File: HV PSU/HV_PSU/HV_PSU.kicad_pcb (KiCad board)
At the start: 2 copper layers, 200 x 80 mm, 104 parts, among them J1 Screw_Terminal_01x07, J13 MountingHole_Pad, J2 AC_HV_1, J3 AC_HV_2, J4 MountingHole_Pad, J5 AC_HV_2, Q1 2N7002, Q2 IRFS4227, Q3 IRFS4227, T1 UY12, U1 L7812, U2 TPS2814D

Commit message: backup
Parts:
- added C19: 330n, Capacitor_THT:C_Rect_L18.0mm_W9.0mm_P15.00mm_FKS3_FKP3, B.Cu at (11.5, 41.5)
- renumbered C19 to C20
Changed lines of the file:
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@@
     (property "Sheetname" "")
     (attr through_hole)
-    (fp_text reference "C19" (at 5 -12.25 90) (layer "F.SilkS")
+    (fp_text reference "C20" (at 5 -12.25 90) (layer "F.SilkS")
       (effects (font (size 1 1) (thickness 0.15)))
     )
@@
     (pad "1" thru_hole circle (at 0 0 270) (size 2.4 2.4) (drill 1.2) (layers *.Cu *.Mask)
       (net 15 "/T_A") (pintype "passive"))
+    (pad "2" thru_hole circle (at 15 0 270) (size 2.4 2.4) (drill 1.2) (layers *.Cu *.Mask)
+      (net 16 "/T_B") (pintype "passive"))
+    (model "${KICAD6_3DMODEL_DIR}/Capacitor_THT.3dshapes/C_Rect_L18.0mm_W9.0mm_P15.00mm_FKS3_FKP3.wrl"
+      (offset (xyz 0 0 0))
+      (scale (xyz 1 1 1))
+      (rotate (xyz 0 0 0))
+    )
+  )
+  (footprint "Capacitor_THT:C_Rect_L18.0mm_W9.0mm_P15.00mm_FKS3_FKP3" (layer "B.Cu")
+    (at 11.5 41.5 -90)
+    (descr "C, Rect series, Radial, pin pitch=15.00mm, , length*width=18*9mm^2, Capacitor, http://www.wima.com/EN/WIMA_FKS_3.pdf")
+    (tags "C Rect series Radial pin pitch 15.00mm  length 18mm width 9mm Capacitor")
+    (property "Sheetfile" "HV_PSU.kicad_sch")
+    (property "Sheetname" "")
+    (attr through_hole)
+    (fp_text reference "C19" (at 7.5 5.75 90) (layer "B.SilkS")
+      (effects (font (size 1 1) (thickness 0.15)) (justify mirror))
+    )
+    (fp_text value "330n" (at 7.5 -5.75 90) (layer "B.Fab")
+      (effects (font (size 1 1) (thickness 0.15)) (justify mirror))
+    )
+    (fp_text user "${REFERENCE}" (at 7.5 0 90) (layer "B.Fab")
+      (effects (font (size 1 1) (thickness 0.15)) (justify mirror))
+    )
+    (fp_line (start 16.62 4.62) (end 16.62 -4.62) (layer "B.SilkS") (width 0.12))
+    (fp_line (start -1.62 -4.62) (end 16.62 -4.62) (layer "B.SilkS") (width 0.12))
+    (fp_line (start -1.62 4.62) (end 16.62 4.62) (layer "B.SilkS") (width 0.12))
+    (fp_line (start -1.62 4.62) (end -1.62 -4.62) (layer "B.SilkS") (width 0.12))
+    (fp_line (start -1.75 4.75) (end -1.75 -4.75) (layer "B.CrtYd") (width 0.05))
+    (fp_line (start 16.75 -4.75) (end 16.75 4.75) (layer "B.CrtYd") (width 0.05))
+    (fp_line (start -1.75 -4.75) (end 16.75 -4.75) (layer "B.CrtYd") (width 0.05))
+    (fp_line (start 16.75 4.75) (end -1.75 4.75) (layer "B.CrtYd") (width 0.05))
+    (fp_line (start -1.5 4.5) (end -1.5 -4.5) (layer "B.Fab") (width 0.1))
+    (fp_line (start -1.5 -4.5) (end 16.5 -4.5) (layer "B.Fab") (width 0.1))
+    (fp_line (start 16.5 4.5) (end -1.5 4.5) (layer "B.Fab") (width 0.1))
+    (fp_line (start 16.5 -4.5) (end 16.5 4.5) (layer "B.Fab") (width 0.1))
+    (pad "1" thru_hole circle (at 0 0 270) (size 2.4 2.4) (drill 1.2) (layers *.Cu *.Mask)
+      (net 15 "/T_A") (pintype "passive"))

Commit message: backup
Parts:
- moved C5 17.7 mm to (10.5, 47.0)
- moved U2 15.1 mm to (5.50, 47.0), turned to 0 degrees
- moved R41 4.17 mm to (13.0, 66.0), turned to 90 degrees
- moved R40 4.16 mm to (13.0, 35.0), turned to -90 degrees
- moved D24 2.24 mm to (15.5, 35.0), turned to -90 degrees
- moved D25 1.80 mm to (15.5, 66.0), turned to -90 degrees
- moved R38 1.19 mm to (15.0, 31.5)
- moved R39 0.84 mm to (15.0, 62.5), turned to 0 degrees
- moved D21 0.55 mm to (14.5, 29.0), turned to 0 degrees
- moved D22 0.21 mm to (14.5, 60.0), turned to 0 degrees
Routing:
- net Net-(D21-Pad1): track 0.00 -> 23.6 mm
- net Net-(D22-Pad1): track 0.00 -> 18.1 mm
- net Net-(D21-Pad2): track 0.00 -> 12.1 mm
- net Net-(D22-Pad2): track 0.00 -> 7.14 mm

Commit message: backup
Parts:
- moved C3 41.2 mm to (14.0, 73.0)
- moved R1 41.0 mm to (11.0, 73.0)
- moved D23 32.0 mm to (7.00, 50.8)
- moved R4 30.2 mm to (2.00, 47.2), turned to 0 degrees
- moved D20 23.0 mm to (7.00, 31.8)
- moved R43 21.7 mm to (1.00, 50.0), turned to -90 degrees
- moved D1 17.2 mm to (6.50, 35.5), turned to 0 degrees
- moved R42 16.2 mm to (1.00, 31.6), turned to 90 degrees
- moved Q1 10.6 mm to (-9.25, 35.5)
- moved R3 7.19 mm to (2.00, 35.5), turned to 0 degrees
- moved U2 7.19 mm to (5.50, 39.8)
- moved C5 5.71 mm to (6.00, 43.5), turned to 0 degrees
- moved C4 3.81 mm to (22.8, 74.7), turned to -90 degrees
- moved R39 2.50 mm to (15.0, 65.0)
- moved D22 2.50 mm to (14.5, 62.5)
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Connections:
- J1 pad 1: VBUS -> GND
- J1 pad 2: VBUS -> GND
- J1 pad 3: VCC -> Net-(J1-Pad3)
- J1 pad 5: Net-(J1-Pad5) -> VCC
- J1 pad 6: GND -> VBUS
- J1 pad 7: GND -> VBUS
- R1 pad 2: Net-(J1-Pad5) -> Net-(J1-Pad3)
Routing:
- net Net-(C3-Pad1): track 0.00 -> 26.7 mm
- net +12V: track 0.00 -> 19.8 mm
- net Net-(D1-Pad1): track 0.00 -> 14.6 mm
- net Net-(D2-Pad1): track 0.00 -> 12.7 mm
- net Net-(J1-Pad3): track 0.00 -> 11.8 mm
- net Net-(D22-Pad1): track 18.1 -> 28.9 mm
- net /T_A: track 0.00 -> 10.4 mm
- net Net-(D22-Pad2): track 7.14 -> 12.2 mm
- net VCC: track 0.00 -> 4.28 mm
- net Net-(D20-Pad2): track 0.00 -> 3.54 mm
- net Net-(D23-Pad2): track 0.00 -> 3.17 mm
- net Net-(D21-Pad1): track 23.6 -> 20.5 mm
- added copper zone on B.Cu, net /T_A
- added copper zone on F.Cu, net /T_A
- added copper zone on B.Cu, net /T_B
- added copper zone on F.Cu, net /T_B

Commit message: backup
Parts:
- moved R43 4.12 mm to (3.00, 46.4)
- moved R4 3.80 mm to (5.80, 47.4)
- moved R42 2.60 mm to (1.00, 29.0)
- moved R3 2.51 mm to (1.00, 33.2), turned to -90 degrees
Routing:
- net Net-(C3-Pad1): track 26.7 -> 35.6 mm
- net +12V: track 19.8 -> 26.7 mm
- net Net-(D20-Pad2): track 3.54 -> 4.95 mm
- net Net-(D23-Pad2): track 3.17 -> 3.89 mm
- net Net-(D1-Pad1): track 14.6 -> 14.1 mm

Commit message: Some routing done
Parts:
- moved R2 47.4 mm to (11.4, 73.3)
- moved D2 23.1 mm to (1.80, 46.0)
- moved Q1 11.5 mm to (2.20, 36.0), turned to 180 degrees
- moved R3 7.80 mm to (1.00, 41.0)
- moved R1 4.95 mm to (10.3, 68.1), turned to 90 degrees
- moved R42 3.20 mm to (1.00, 32.2)
- moved C3 3.05 mm to (11.4, 71.4), turned to 0 degrees
- moved C5 1.31 mm to (6.85, 44.5)
- moved U2 1.00 mm to (5.50, 40.8)
- moved R4 0.85 mm to (6.65, 47.4)
- moved R43 0.85 mm to (3.85, 46.4)
- moved D1 0.71 mm to (7.00, 36.0)
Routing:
- net Net-(C3-Pad1): track 35.6 -> 47.1 mm
- net +12V: track 26.7 -> 34.8 mm
- net Net-(D22-Pad1): track 28.7 -> 22.1 mm
- net Net-(J1-Pad3): track 11.8 -> 5.71 mm
- net Net-(D2-Pad1): track 13.1 -> 16.2 mm
- net Net-(D20-Pad2): track 4.95 -> 3.29 mm
- net Net-(D21-Pad1): track 20.5 -> 21.1 mm

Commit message: Some more routing
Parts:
- moved C4 5.95 mm to (16.8, 74.5), turned to 0 degrees
- moved C20 5.84 mm to (33.5, 88.2), turned to 90 degrees
- turned R2 to 0 degrees
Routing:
- net +12V: track 34.8 -> 72.6 mm, vias 0 -> 3
- net VCC: track 4.28 -> 18.6 mm, vias 0 -> 2
- net Net-(D22-Pad1): track 22.1 -> 28.7 mm
- net Net-(D22-Pad2): track 12.2 -> 14.1 mm
- net Net-(C3-Pad1): track 47.1 -> 46.0 mm
- net Net-(D1-Pad1): track 13.9 -> 14.8 mm
- added copper zone on F.Cu, net /T_TAP
- added copper zone on B.Cu, net VBUS

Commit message: Done routing - round 1
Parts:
- moved J2 0.27 mm to (114.0, 51.2)
- moved J3 0.27 mm to (114.0, 83.2)
- turned R44 to 180 degrees
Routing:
- net Net-(C7-Pad1): track 0.00 -> 35.7 mm
- net Net-(C6-Pad2): track 0.00 -> 22.1 mm
- net Net-(C7-Pad2): track 0.00 -> 18.8 mm
- net Net-(C11-Pad1): track 0.00 -> 18.5 mm
- net Net-(C11-Pad2): track 0.00 -> 17.8 mm
- net Net-(C10-Pad2): track 0.00 -> 17.3 mm
- net Net-(C10-Pad1): track 0.00 -> 16.9 mm
- net GND1: track 0.00 -> 12.9 mm
- net /HV_OUT: track 0.00 -> 12.6 mm
- net Net-(C12-Pad2): track 0.00 -> 12.4 mm
- net GND: track 0.00 -> 11.4 mm, vias 0 -> 42
- net /HV_AC: track 0.00 -> 7.11 mm
- net Net-(D9-Pad1): track 0.00 -> 3.63 mm
- net Net-(D5-Pad1): track 0.00 -> 3.36 mm
- net Net-(D7-Pad2): track 0.00 -> 3.34 mm
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- added copper zone on B.Cu, net GND
- added copper zone on F.Cu, net GND
- added copper zone on F.Cu, net VBUS
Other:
- outline, holes or cut-outs redrawn
- board text added: "+12V"
- board text added: "/EN"
- board text added: "GND"
- board text added: "REGIN"
- board text added: "UHV-PSU Rev A - 2448A Hannah Hoaglund Tom Wimmenhove"
- board text added: "VBUS"

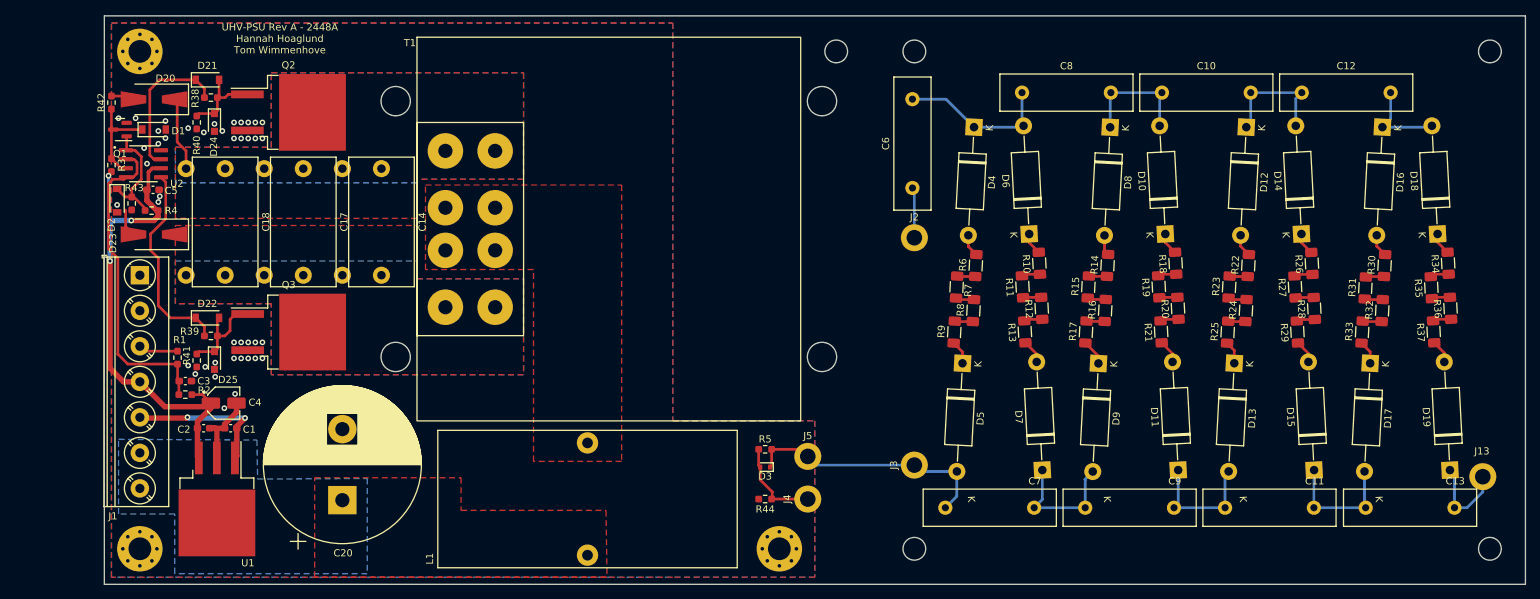
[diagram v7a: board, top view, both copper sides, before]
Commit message: Cleanup of RefDes
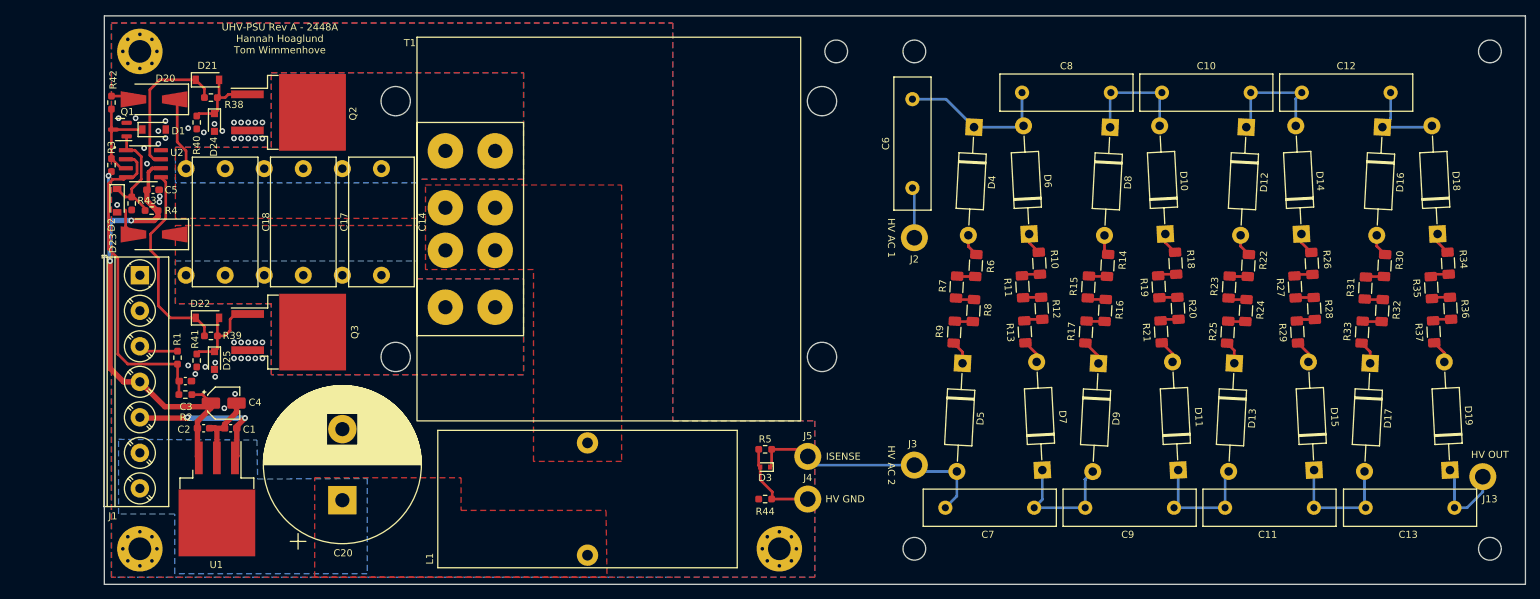
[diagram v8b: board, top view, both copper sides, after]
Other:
- board text added: "HV AC 1"
- board text added: "HV AC 2"
- board text added: "HV GND"
- board text added: "HV OUT"
- board text added: "ISENSE"
